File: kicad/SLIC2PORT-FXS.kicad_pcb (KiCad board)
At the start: 2 copper layers, 120 x 90 mm, 160 parts, among them J1 USB-C_PWR, J2 DC5V_IN, J5 EXPANSION, J6 UART_DBG, K1 G5V-2_DC5, K2 G5V-2_DC5, Q1 AO3401A, Q2 2N7002, Q3 2N7002, Q4 2N7002, Q5 2N7002, Q6 2N7002, SW1 RST, SW2 BOOT, U1 M5StampS3/S3A, U106 1N5819, U2 74HCT244, U45 1N4007, U49 1N4007, U55 P3100SC, U56 1N4007, U57 1N4007, U58 1N4007, U59 1N4007, U60 BZT03C82, U64 BK2125HS601-T, U79 1N5819, U82 P3100SC, U83 1N4007, U84 1N4007, U85 1N4007, U86 1N4007, U87 BZT03C82, U91 BK2125HS601-T

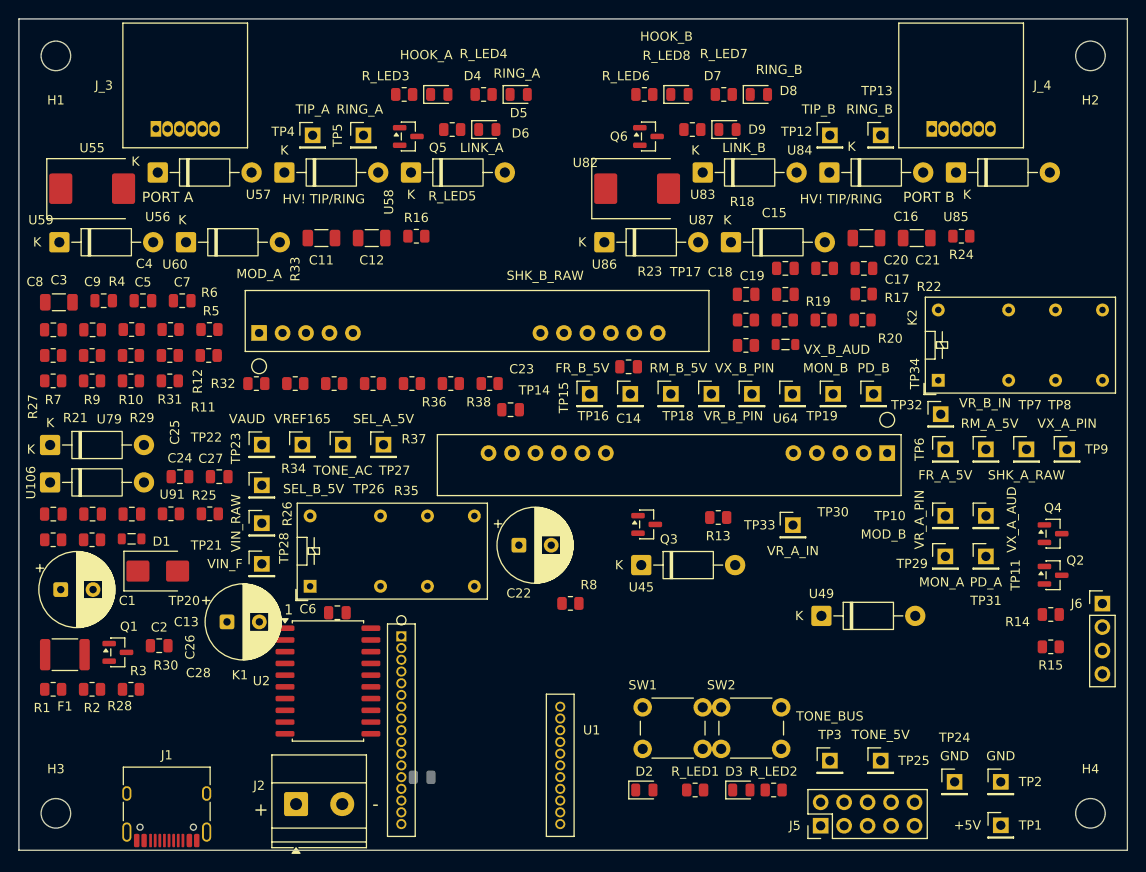
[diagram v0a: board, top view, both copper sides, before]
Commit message: board v3.4.1: SW2 移動・保護ネット是正・RJ11 パッド縮小 (Issue #9)
v3.4 からの差分はこの3点のみ (全配置・全パッドネットを機械比較済み):
1. SW2 を +1.8mm (X) へ移動: SW1 pin1 (EN) と SW2 pin1 (GPIO0) の
   Ø2.0 パッドが中心間 2.0mm で接触 (間隔 0mm) していた問題を解消し
   間隔 1.8mm を確保。EasyEDA DRC でも 0mil 接触として検出されていた。
2. 保護回路: U58/U59/U60/U85/U86/U87 pin2 を BRM_x -> GND (メーカー図
   の GND 基準クランプに一致。生成元 SKiDL と同期済み)。
3. RJ11 (J_3/J_4) パッド幅 1.15 -> 1.13mm: 間隔 0.14mm (JLC 最小
   0.127 以上) / 環状銅箔 0.19mm (同 0.18 以上)。
ネットは番号付き標準形式を維持 (82 nets)。
注意: EasyEDA で配線済みの v3.4 データ (b0964c9) とは SW2 位置・保護
ネット・RJ11 パッドが異なるため、配線側は v3.4.1 の再取り込みが必要。
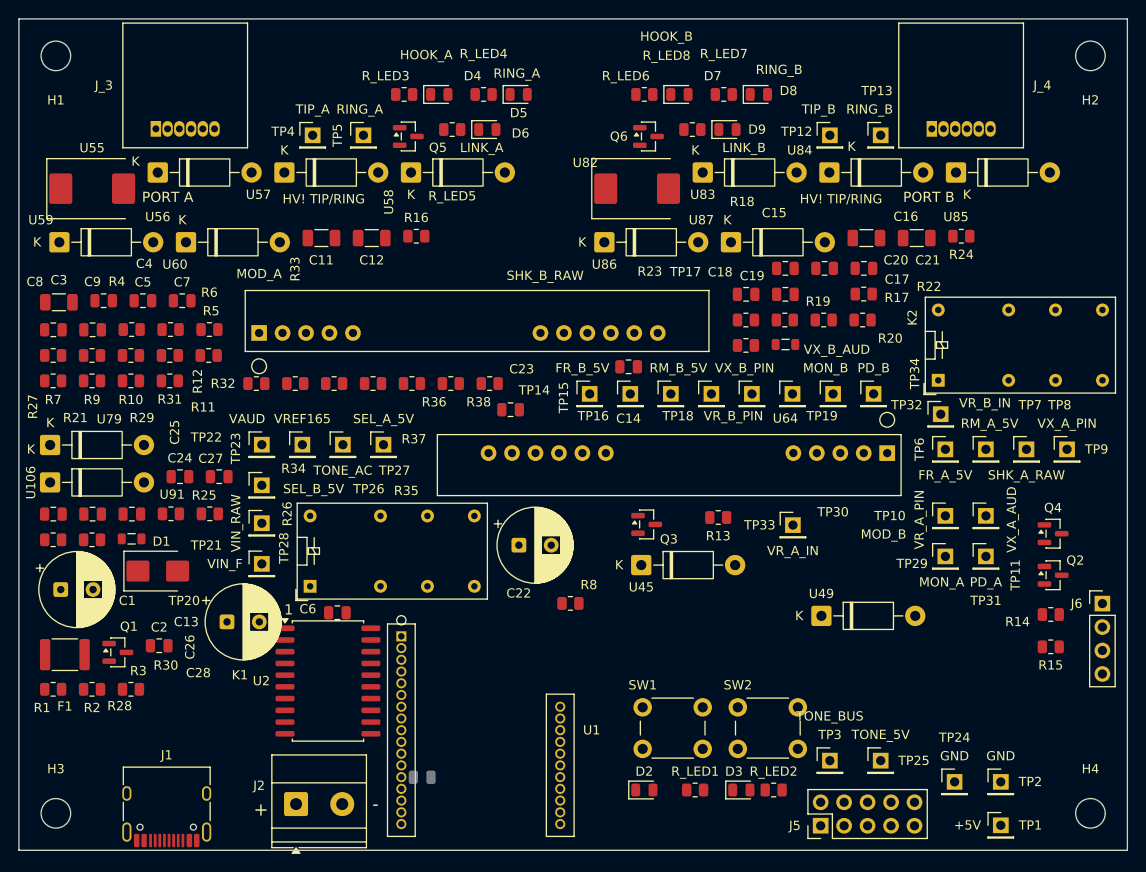
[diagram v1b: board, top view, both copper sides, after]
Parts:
- moved SW2 1.80 mm to (77.8, 74.5)
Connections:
- U58 pad 2: BRM_A -> GND
- U59 pad 2: BRM_A -> GND
- U60 pad 2: BRM_A -> GND
- U85 pad 2: BRM_B -> GND
- U86 pad 2: BRM_B -> GND
- U87 pad 2: BRM_B -> GND
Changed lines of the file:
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@@
 	(net 69 "VR_A_PIN")
 	(net 70 "TONE_BUS")
-	(net 71 "BRM_B")
-	(net 72 "LED_LK_B")
-	(net 73 "HK_A_DRV")
-	(net 74 "LED_LK_A")
-	(net 75 "VX_A_PIN")
-	(net 76 "LED_HK_A")
-	(net 77 "VX_B_AUD")
-	(net 78 "VX_B_IN")
-	(net 79 "LED_PWR_A")
-	(net 80 "Q1_GATE")
-	(net 81 "LED_ST_A")
-	(net 82 "VR_B_PIN")
-	(net 83 "PD_BUS")
-	(net 84 "BRM_A")
+	(net 71 "LED_LK_B")
+	(net 72 "HK_A_DRV")
+	(net 73 "LED_LK_A")
+	(net 74 "VX_A_PIN")
+	(net 75 "LED_HK_A")
+	(net 76 "VX_B_AUD")
+	(net 77 "VX_B_IN")
+	(net 78 "LED_PWR_A")
+	(net 79 "Q1_GATE")
+	(net 80 "LED_ST_A")
+	(net 81 "VR_B_PIN")
+	(net 82 "PD_BUS")
 	(footprint "RJ11_6P6C_TH"
 		(layer "F.Cu")
@@
 		(pad "1" thru_hole rect
 			(at -3.175 4.7)
-			(size 1.15 1.7)
+			(size 1.13 1.7)
 			(drill 0.75)
 			(layers "*.Cu" "*.Mask")
@@
 		(pad "2" thru_hole oval
 			(at -1.905 4.7)
-			(size 1.15 1.7)
+			(size 1.13 1.7)
 			(drill 0.75)
 			(layers "*.Cu" "*.Mask")
@@
 		(pad "3" thru_hole oval
 			(at -0.635 4.7)
-			(size 1.15 1.7)
+			(size 1.13 1.7)
 			(drill 0.75)
 			(layers "*.Cu" "*.Mask")
@@
 		(pad "4" thru_hole oval
 			(at 0.635 4.7)
-			(size 1.15 1.7)
+			(size 1.13 1.7)
 			(drill 0.75)
 			(layers "*.Cu" "*.Mask")
@@
 		(pad "5" thru_hole oval
 			(at 1.905 4.7)
-			(size 1.15 1.7)
+			(size 1.13 1.7)
 			(drill 0.75)
 			(layers "*.Cu" "*.Mask")
@@
 		(pad "6" thru_hole oval
 			(at 3.175 4.7)
-			(size 1.15 1.7)
+			(size 1.13 1.7)
 			(drill 0.75)
 			(layers "*.Cu" "*.Mask")
@@
 	(footprint "SW_PUSH_6mm"
 		(layer "F.Cu")
-		(at 76.025 74.525)
+		(at 77.825 74.525)
 		(descr "Generic 6mm SW tactile push button")
 		(tags "tact sw push 6mm")
@@
 			(layers "*.Cu" "*.Mask")
 			(remove_unused_layers no)
-			(net 71 "BRM_B")
+			(net 4 "GND")
 		)
 		(embedded_fonts no)
@@
 			(layers "F.Cu" "F.Mask" "F.Paste")
 			(roundrect_rratio 0.25)
-			(net 72 "LED_LK_B")
+			(net 71 "LED_LK_B")
 		)
 		(embedded_fonts no)
@@
 			(layers "F.Cu" "F.Mask" "F.Paste")
 			(roundrect_rratio 0.25)
-			(net 73 "HK_A_DRV")
+			(net 72 "HK_A_DRV")
 		)
 		(embedded_fonts no)
@@
 			(layers "F.Cu" "F.Mask" "F.Paste")
 			(roundrect_rratio 0.25)
-			(net 74 "LED_LK_A")
+			(net 73 "LED_LK_A")
 		)
 		(embedded_fonts no)
@@
 			(layers "*.Cu" "*.Mask")
 			(remove_unused_layers no)
-			(net 75 "VX_A_PIN")
+			(net 74 "VX_A_PIN")
 		)
 		(pad "8" thru_hole circle
@@
 			(layers "F.Cu" "F.Mask" "F.Paste")
 			(roundrect_rratio 0.25)
-			(net 73 "HK_A_DRV")
+			(net 72 "HK_A_DRV")
 		)
 		(pad "2" smd roundrect
@@
 			(layers "F.Cu" "F.Mask" "F.Paste")
 			(roundrect_rratio 0.25)
-			(net 76 "LED_HK_A")
+			(net 75 "LED_HK_A")
 		)
 		(embedded_fonts no)
@@
 			(layers "*.Cu" "*.Mask")
 			(remove_unused_layers no)
-			(net 77 "VX_B_AUD")
+			(net 76 "VX_B_AUD")
 		)
 		(embedded_fonts no)
@@
 			(layers "F.Cu" "F.Mask" "F.Paste")
 			(roundrect_rratio 0.243902)
-			(net 76 "LED_HK_A")
+			(net 75 "LED_HK_A")
 		)
 		(embedded_fonts no)
@@
 			(layers "*.Cu" "*.Mask")
 			(remove_unused_layers no)
-			(net 75 "VX_A_PIN")
+			(net 74 "VX_A_PIN")
 		)
 		(embedded_fonts no)
@@
 			(layers "*.Cu" "*.Mask")
 			(remove_unused_layers no)
-			(net 78 "VX_B_IN")
+			(net 77 "VX_B_IN")
 		)
 		(pad "8" thru_hole circle
@@
 			(layers "*.Cu" "*.Mask")
 			(remove_unused_layers no)
-			(net 78 "VX_B_IN")
+			(net 77 "VX_B_IN")
 		)
 		(pad "13" thru_hole circle
@@
 			(layers "F.Cu" "F.Mask" "F.Paste")
 			(roundrect_rratio 0.25)
-			(net 79 "LED_PWR_A")
+			(net 78 "LED_PWR_A")
 		)
 		(embedded_fonts no)
@@
 			(layers "F.Cu" "F.Mask" "F.Paste")
 			(roundrect_rratio 0.243902)
-			(net 80 "Q1_GATE")
+			(net 79 "Q1_GATE")
 		)
 		(pad "2" smd roundrect
@@
 			(layers "F.Cu" "F.Mask" "F.Paste")
 			(roundrect_rratio 0.243902)
-			(net 81 "LED_ST_A")
+			(net 80 "LED_ST_A")
 		)
 		(embedded_fonts no)
@@
 			(layers "*.Cu" "*.Mask")
 			(remove_unused_layers no)
-			(net 82 "VR_B_PIN")
+			(net 81 "VR_B_PIN")
 		)
 		(embedded_fonts no)
@@
 			(layers "F.Cu" "F.Mask" "F.Paste")
 			(roundrect_rratio 0.25)
-			(net 77 "VX_B_AUD")
+			(net 76 "VX_B_AUD")
 		)
 		(embedded_fonts no)
@@
 			(remove_unused_layers no)
 			(roundrect_rratio 0.113636)
-			(net 83 "PD_BUS")
+			(net 82 "PD_BUS")
 		)
 		(pad "2" thru_hole circle
@@
 			(layers "*.Cu" "*.Mask")
 			(remove_unused_layers no)
-			(net 71 "BRM_B")
+			(net 4 "GND")
 		)
 		(embedded_fonts no)
@@
 			(layers "*.Cu" "*.Mask")
 			(remove_unused_layers no)
-			(net 71 "BRM_B")
+			(net 4 "GND")
 		)
 		(embedded_fonts no)
@@
 			(layers "F.Cu" "F.Mask" "F.Paste")
 			(roundrect_rratio 0.243902)
-			(net 79 "LED_PWR_A")
+			(net 78 "LED_PWR_A")
 		)
 		(embedded_fonts no)
@@
 			(layers "F.Cu" "F.Mask" "F.Paste")
 			(roundrect_rratio 0.25)
-			(net 83 "PD_BUS")
+			(net 82 "PD_BUS")
 		)
 		(embedded_fonts no)
@@
 			(layers "F.Cu" "F.Mask" "F.Paste")
 			(roundrect_rratio 0.25)
-			(net 77 "VX_B_AUD")
+			(net 76 "VX_B_AUD")
 		)
 		(pad "2" smd roundrect
@@
 			(layers "F.Cu" "F.Mask" "F.Paste")
 			(roundrect_rratio 0.25)
-			(net 75 "VX_A_PIN")
+			(net 74 "VX_A_PIN")
 		)
 		(pad "2" smd roundrect
@@
 			(layers "*.Cu" "*.Mask")
 			(remove_unused_layers no)
-			(net 84 "BRM_A")
+			(net 4 "GND")
 		)
 		(embedded_fonts no)
@@
 			(remove_unused_layers no)
 			(roundrect_rratio 0.113636)
-			(net 83 "PD_BUS")
+			(net 82 "PD_BUS")
 		)
 		(pad "2" thru_hole circle
@@
 		(pad "1" thru_hole rect
 			(at -3.175 4.7)
-			(size 1.15 1.7)
+			(size 1.13 1.7)
 			(drill 0.75)
 			(layers "*.Cu" "*.Mask")
@@
 		(pad "2" thru_hole oval
 			(at -1.905 4.7)
-			(size 1.15 1.7)
+			(size 1.13 1.7)
 			(drill 0.75)
 			(layers "*.Cu" "*.Mask")
@@
 		(pad "3" thru_hole oval
 			(at -0.635 4.7)
-			(size 1.15 1.7)
+			(size 1.13 1.7)
 			(drill 0.75)
 			(layers "*.Cu" "*.Mask")
@@
 		(pad "4" thru_hole oval
 			(at 0.635 4.7)
-			(size 1.15 1.7)
+			(size 1.13 1.7)
 			(drill 0.75)
 			(layers "*.Cu" "*.Mask")
@@
 		(pad "5" thru_hole oval
 			(at 1.905 4.7)
-			(size 1.15 1.7)
+			(size 1.13 1.7)
 			(drill 0.75)
 			(layers "*.Cu" "*.Mask")
@@
 		(pad "6" thru_hole oval
 			(at 3.175 4.7)
-			(size 1.15 1.7)
+			(size 1.13 1.7)
 			(drill 0.75)
 			(layers "*.Cu" "*.Mask")
@@
 			(layers "F.Cu" "F.Mask" "F.Paste")
 			(roundrect_rratio 0.243902)
-			(net 77 "VX_B_AUD")
+			(net 76 "VX_B_AUD")
 		)
 		(pad "2" smd roundrect
@@
 			(layers "F.Cu" "F.Mask" "F.Paste")
 			(roundrect_rratio 0.25)
-			(net 81 "LED_ST_A")
+			(net 80 "LED_ST_A")
 		)
 		(embedded_fonts no)
@@
 			(layers "F.Cu" "F.Mask" "F.Paste")
 			(roundrect_rratio 0.243902)
-			(net 72 "LED_LK_B")
+			(net 71 "LED_LK_B")
 		)
 		(embedded_fonts no)
@@
 			(layers "F.Cu" "F.Mask" "F.Paste")
 			(roundrect_rratio 0.243902)
-			(net 74 "LED_LK_A")
+			(net 73 "LED_LK_A")
 		)
 		(embedded_fonts no)
@@
 			(layers "F.Cu" "F.Mask" "F.Paste")
 			(roundrect_rratio 0.25)
-			(net 80 "Q1_GATE")
+			(net 79 "Q1_GATE")
 		)
 		(pad "2" smd roundrect
@@
 			(layers "F.Cu" "F.Mask" "F.Paste")
 			(roundrect_rratio 0.25)
-			(net 82 "VR_B_PIN")
+			(net 81 "VR_B_PIN")
 		)
 		(embedded_fonts no)
@@
 			(layers "*.Cu" "*.Mask")
 			(remove_unused_layers no)
-			(net 82 "VR_B_PIN")
+			(net 81 "VR_B_PIN")
 		)
 		(pad "7" thru_hole circle
@@
 			(layers "*.Cu" "*.Mask")
 			(remove_unused_layers no)
-			(net 84 "BRM_A")
+			(net 4 "GND")
 		)
 		(embedded_fonts no)
@@
 			(layers "F.Cu" "F.Mask" "F.Paste")
 			(roundrect_rratio 0.243902)
-			(net 77 "VX_B_AUD")
+			(net 76 "VX_B_AUD")
 		)
 		(pad "2" smd roundrect
@@
 			(layers "F.Cu" "F.Mask" "F.Paste")
 			(roundrect_rratio 0.243902)
-			(net 78 "VX_B_IN")
+			(net 77 "VX_B_IN")
 		)
 		(embedded_fonts no)
@@
 			(layers "*.Cu" "*.Mask")
 			(remove_unused_layers no)
-			(net 84 "BRM_A")
+			(net 4 "GND")
 		)
 		(embedded_fonts no)

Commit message: board v3.4.2: RJ11 を Neltron 7002 実寸へ是正し保護部品9点を移設
- J_3/J_4: フットプリントを千鳥2列+ペグ穴へ差し替え、原点 (ペグ中心線)
  を y 7.2 -> 6.45 へ (開口面は基板端から 0.45mm を維持、本体奥行 15.0)
- 本体が 1.5mm 深くなり旧保護1列目と干渉するため、干渉する保護部品
  9点を純粋平行移動で退避 (U56/U84/U85 は2列目へ、C11/C12/R16/C20 は
  列間の空き帯へ、C21/R24 は2列目の下へ)。生成元 build_pcb_v32.py に
  round 9 として同期し check_regen は警告0/エラー0
- ネット・未接続数 (295) は不変、物理干渉 (Fab/パッド) 0件を確認。
  コートヤード新規重なりは J_3-U55 の1組のみ (本体間 0.37mm、裁定OK)
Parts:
- moved U56 18.6 mm to (32.0, 24.2)
- moved U84 8.24 mm to (91.0, 24.2)
- moved U85 8.04 mm to (104.2, 24.2)
- moved R24 4.45 mm to (102.0, 28.0)
- moved C21 4.37 mm to (97.2, 28.1)
- moved C11 3.98 mm to (32.7, 19.7)
- moved C12 3.98 mm to (38.2, 19.7)
- moved C20 3.98 mm to (91.7, 19.7)
- moved R16 3.90 mm to (43.0, 19.6)
- moved J_3 0.75 mm to (18.0, 6.45)
- moved J_4 0.75 mm to (102.0, 6.45)
